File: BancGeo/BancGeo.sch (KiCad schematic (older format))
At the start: 114 parts, among them P1 Alim, P2 Batt, P3 CONN_01X05, P4 Capt1, P5 Capt2, P6 Capt3, P7 Capt4, P8 USB_D-, P9 USB_D+, Q1 2N7002E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

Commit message: Update Bancgeo
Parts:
- added R36: nc, Yame_library:SM0603-MR, symbol R
- D3, D4, D5, D7, D8, D9: footprint LEDs:LED-5MM -> Yame_library:LED-5MM_center
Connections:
- wire segments 374 -> 405
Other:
- moved on the sheet: R38, R39, R40, R41, R42, R43

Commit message: Update BancGeo
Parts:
- added C36: 100n, Yame_library:SM0603-MR, symbol C
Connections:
- net labels added: Self_Out_1, Self_Out_2, TR_High_Side, TR_Low_Side
- wire segments 405 -> 406
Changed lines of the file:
@@
 $EndComp
 Text Label 4150 4650 0    60   ~ 0
-+Vref1
++Vref2
 $Comp
 L R R11
@@
 	4050 1050 4300 1050
 Wire Wire Line
-	4700 900  4700 1050
+	4700 900  4700 1150
 Wire Wire Line
 	4700 1050 4600 1050
@@
 Wire Wire Line
 	13000 1700 12950 1700
+$Comp
+L C C36
+U 1 1 573E302E
+P 4700 1300
+F 0 "C36" H 4725 1400 50  0000 L CNN
+F 1 "100n" H 4725 1200 50  0000 L CNN
+F 2 "Yame_library:SM0603-MR" H 4738 1150 30  0001 C CNN
+F 3 "" H 4700 1300 60  0000 C CNN
+	1    4700 1300
+	1    0    0    -1
+$EndComp
+$Comp
+L GND #PWR070
+U 1 1 573E3034
+P 4700 1550
+F 0 "#PWR070" H 4700 1300 50  0001 C CNN
+F 1 "GND" H 4700 1400 50  0000 C CNN
+F 2 "" H 4700 1550 60  0000 C CNN
+F 3 "" H 4700 1550 60  0000 C CNN
+	1    4700 1550
+	1    0    0    -1
+$EndComp
+Wire Wire Line
+	4700 1450 4700 1550
+Connection ~ 4700 1050
+Text Label 5700 8000 0    60   ~ 0
+TR_Low_Side
+Text Label 5700 7300 0    60   ~ 0
+TR_High_Side
+Text Label 6350 7400 0    60   ~ 0
+Self_Out_2
+Text Label 6850 7900 0    60   ~ 0
+Self_Out_1
 $EndSCHEMATC

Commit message: Update BancGeo
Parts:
- added P10: GND, Yame_library:Test_Point_T_H, symbol CONN_01X01
- added Q6: 2N7002E, Yame_library:SOT23-MR, symbol N-MOS_SOT23
- added R37, R44: 100k, Yame_library:SM0603-MR, symbol R
- P1, P2: footprint Connect:PINHEAD1-2 -> Yame_library:PINHEAD1-2
- P4, P5, P6, P7: footprint Connect:PINHEAD1-3 -> Yame_library:PINHEAD1-3
- R1: value 10k -> 100k
- U3: value MCP6541 -> MCP6546
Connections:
- wire segments 406 -> 407
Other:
- moved on the sheet: Q1, R1

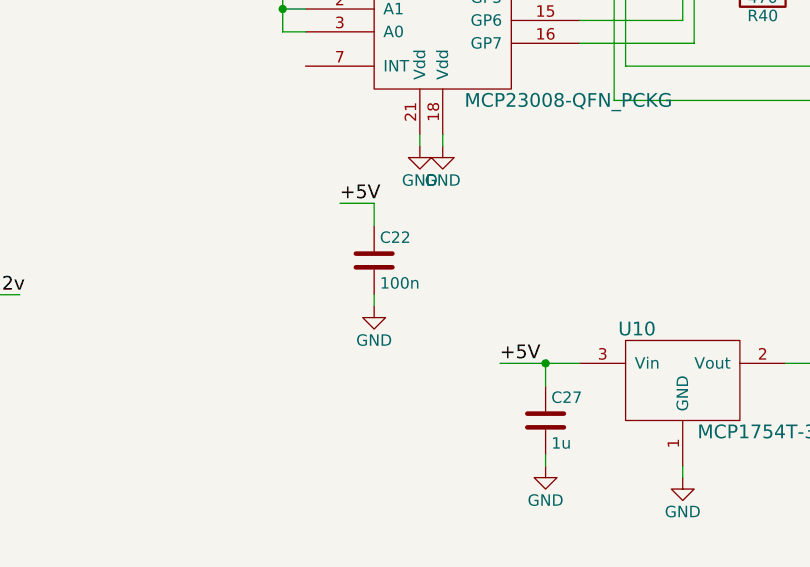
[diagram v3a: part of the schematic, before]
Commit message: Change C22 value
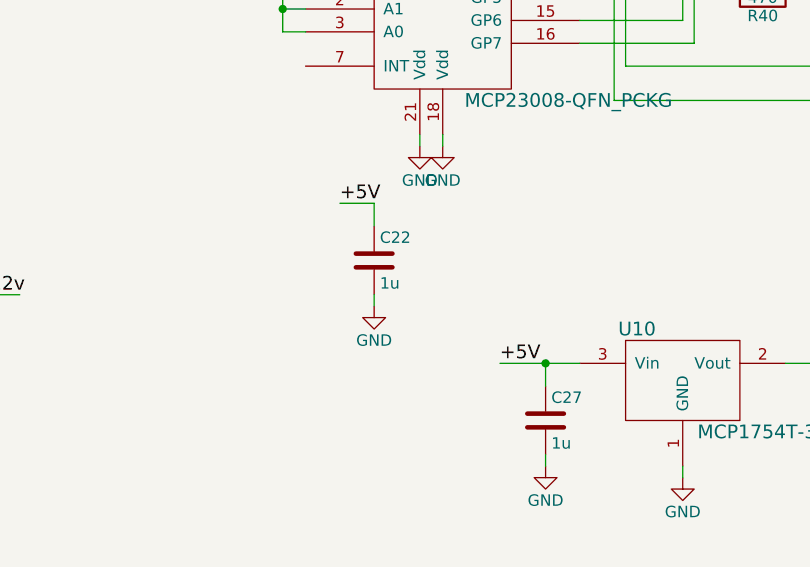
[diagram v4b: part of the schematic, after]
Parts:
- C22: value 100n -> 1u
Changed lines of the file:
@@
 P 12050 2950
 F 0 "C22" H 12075 3050 50  0000 L CNN
-F 1 "100n" H 12075 2850 50  0000 L CNN
+F 1 "1u" H 12075 2850 50  0000 L CNN
 F 2 "Yame_library:SM0805-MR" H 12088 2800 30  0001 C CNN
 F 3 "" H 12050 2950 60  0000 C CNN

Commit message: update Bancgeo.sch
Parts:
- U6: value MCP1631X-ML_QFN -> MCP1631V-ML_QFN
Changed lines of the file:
@@
 P 4950 9500
 F 0 "U6" H 2650 10850 60  0000 C CNN
-F 1 "MCP1631X-ML_QFN" H 3600 9050 60  0000 C CNN
+F 1 "MCP1631V-ML_QFN" H 3600 9050 60  0000 C CNN
 F 2 "Housings_DFN_QFN:QFN-20-1EP_4x4mm_Pitch0.5mm" H 4950 9500 60  0001 C CNN
 F 3 "" H 4950 9500 60  0000 C CNN

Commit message: Update BancGeo alim feed
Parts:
- added D? (x2): PDS760-13, symbol DIODE_SCHOTTKY_3PIN
- added Q?: P-MOS_SOIC, symbol P-MOS_SOIC
- added R?: 100k, symbol R
- D3, D4, D5, D6, D7, D8, D9: symbol LED -> LED-RESCUE-BancGeo
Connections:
- net labels added: +Vfeed
- wire segments 407 -> 426
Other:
- moved on the sheet: P2
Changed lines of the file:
@@
 EESchema Schematic File Version 2
+LIBS:BancGeo-rescue
 LIBS:power
 LIBS:device
@@
 Text Label 10300 3100 0    60   ~ 0
 +12v
-Text Label 7250 5400 0    60   ~ 0
+Text Label 2200 3300 0    60   ~ 0
 +Vbat
 $Comp
@@
 L CONN_01X02 P2
 U 1 1 56B94194
-P 1100 3850
-F 0 "P2" H 1100 4000 50  0000 C CNN
-F 1 "Batt" V 1200 3850 50  0000 C CNN
-F 2 "Yame_library:PINHEAD1-2" H 1100 3850 60  0001 C CNN
-F 3 "" H 1100 3850 60  0000 C CNN
-	1    1100 3850
+P 800 3850
+F 0 "P2" H 800 4000 50  0000 C CNN
+F 1 "Batt" V 900 3850 50  0000 C CNN
+F 2 "Yame_library:PINHEAD1-2" H 800 3850 60  0001 C CNN
+F 3 "" H 800 3850 60  0000 C CNN
+	1    800  3850
 	-1   0    0    -1
 $EndComp
@@
 $EndComp
 $Comp
-L LED D3
+L LED-RESCUE-BancGeo D3
 U 1 1 56BAE8CB
 P 14550 700
@@
 $EndComp
 $Comp
-L LED D4
+L LED-RESCUE-BancGeo D4
 U 1 1 56BAEA55
 P 14750 950
@@
 $EndComp
 $Comp
-L LED D5
+L LED-RESCUE-BancGeo D5
 U 1 1 56BAF1D5
 P 14950 1200
@@
 $EndComp
 $Comp
-L LED D7
+L LED-RESCUE-BancGeo D7
 U 1 1 56BAF1DB
 P 15100 1450
@@
 $EndComp
 $Comp
-L LED D8
+L LED-RESCUE-BancGeo D8
 U 1 1 56BAF1E1
 P 15300 1700
@@
 $EndComp
 $Comp
-L LED D9
+L LED-RESCUE-BancGeo D9
 U 1 1 56BAF1E7
 P 15500 1950
@@
 $EndComp
 $Comp
-L LED D6
+L LED-RESCUE-BancGeo D6
 U 1 1 56BD4C8C
 P 15000 6650
@@
 	9200 5400 8550 5400
 Wire Wire Line
-	1300 3900 1350 3900
+	1350 2900 1350 4000
 Wire Wire Line
-	1350 3900 1350 4000
-Wire Wire Line
-	1300 3800 2200 3800
+	1000 3800 2200 3800
 Wire Wire Line
 	1400 650  1900 650
@@
 Wire Wire Line
 	13100 1600 13100 2250
+$Comp
+L GND #PWR?
+U 1 1 58A8AD90
+P 1000 4000
+F 0 "#PWR?" H 1000 3750 50  0001 C CNN
+F 1 "GND" H 1000 3850 50  0000 C CNN
+F 2 "" H 1000 4000 60  0000 C CNN
+F 3 "" H 1000 4000 60  0000 C CNN
+	1    1000 4000
+	1    0    0    -1
+$EndComp
+Wire Wire Line
+	1000 3900 1000 4000
+$Comp
+L P-MOS_SOIC Q?
+U 1 1 58A8B1D3
+P 1700 2800
+F 0 "Q?" H 1500 2850 50  0000 L BNN
+F 1 "P-MOS_SOIC" H 1850 2750 50  0000 L BNN
+F 2 "" H 1700 2950 50  0001 C CNN
+F 3 "" H 1700 2800 60  0000 C CNN
+	1    1700 2800
+	1    0    0    -1
+$EndComp
+Wire Wire Line
+	1350 2900 1500 2900
+$Comp
+L R R?
+U 1 1 58A8C1CB
+P 1550 3300
+F 0 "R?" V 1630 3300 50  0000 C CNN
+F 1 "100k" V 1550 3300 50  0000 C CNN
+F 2 "" V 1480 3300 50  0000 C CNN
+F 3 "" H 1550 3300 50  0000 C CNN
+	1    1550 3300
+	0    1    1    0
+$EndComp
+Wire Wire Line
+	1700 3300 2450 3300
+Wire Wire Line
+	1800 3300 1800 3050
+Wire Wire Line
+	1950 3300 1950 3050
+Connection ~ 1800 3300
+Wire Wire Line
+	2100 3300 2100 3050
+Connection ~ 1950 3300
+Wire Wire Line
+	1400 3300 1350 3300
+Connection ~ 1350 3300
+Connection ~ 2100 3300
+Wire Wire Line
+	1800 2550 1800 2450
+Wire Wire Line
+	1800 2450 2450 2450
+Wire Wire Line
+	2250 2550 2250 2450
+Connection ~ 2250 2450
+Wire Wire Line
+	2100 2550 2100 2450
+Connection ~ 2100 2450
+Wire Wire Line
+	1950 2550 1950 2450
+Connection ~ 1950 2450
+Text Label 2300 2450 0    60   ~ 0
++Vfeed
+Text Label 6200 5150 0    60   ~ 0
++Vfeed
+$Comp
+L DIODE_SCHOTTKY_3PIN D?
+U 1 1 58A8F0BC
+P 6950 5600
+F 0 "D?" H 6950 5750 60  0000 C CNN
+F 1 "PDS760-13" H 7050 5450 60  0000 C CNN
+F 2 "" H 6950 5600 60  0000 C CNN
+F 3 "" H 6950 5600 60  0000 C CNN
+	1    6950 5600
+	1    0    0    -1
+$EndComp
+$Comp
+L DIODE_SCHOTTKY_3PIN D?
+U 1 1 58A8F35D
+P 6900 5150
+F 0 "D?" H 6900 5300 60  0000 C CNN
+F 1 "PDS760-13" H 7000 5000 60  0000 C CNN
+F 2 "" H 6900 5150 60  0000 C CNN
+F 3 "" H 6900 5150 60  0000 C CNN
+	1    6900 5150
+	1    0    0    -1
+$EndComp
+Text Label 6200 5600 0    60   ~ 0
++12v
+Wire Wire Line
+	7200 5150 7250 5150
+Wire Wire Line
+	7250 5150 7250 5600
+Connection ~ 7250 5400
+Wire Wire Line
+	6700 5500 6600 5500
+Wire Wire Line
+	6600 5500 6600 5600
+Wire Wire Line
+	6200 5600 6700 5600
+Wire Wire Line
+	6650 5050 6600 5050
+Wire Wire Line
+	6600 5050 6600 5150
+Wire Wire Line
+	6200 5150 6650 5150
+Connection ~ 6600 5600
+Connection ~ 6600 5150
 $EndSCHEMATC

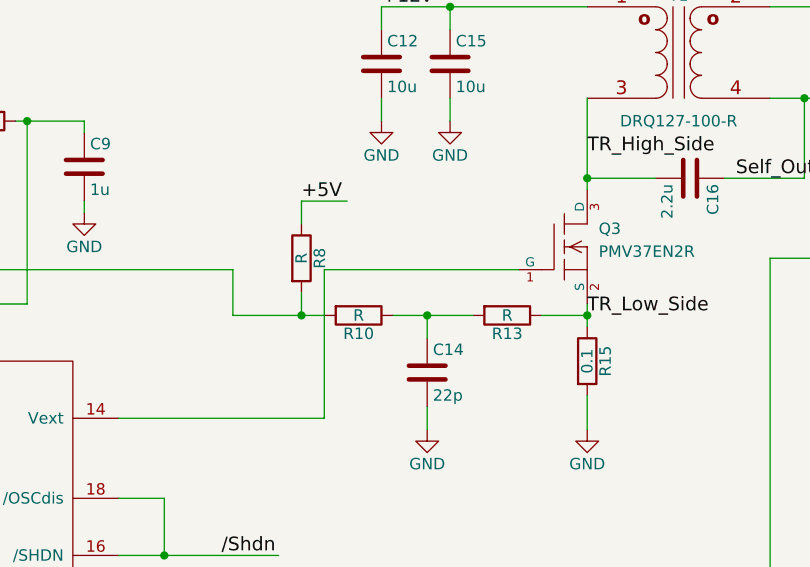
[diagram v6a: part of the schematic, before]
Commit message: Set L1 max current resistance values
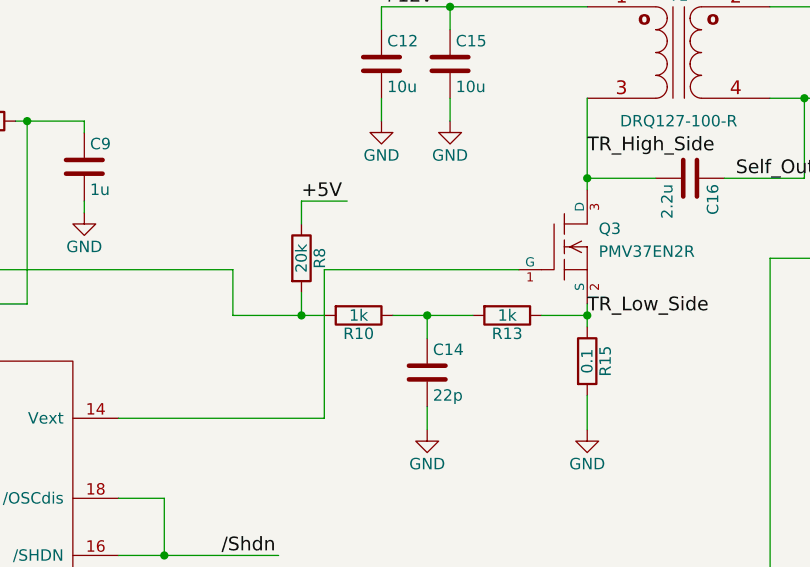
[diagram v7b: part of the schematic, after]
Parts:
- R10, R13: value R -> 1k
- R8: value R -> 20k
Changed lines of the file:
@@
 EESchema Schematic File Version 2
-LIBS:BancGeo-rescue
 LIBS:power
 LIBS:device
@@
 P 5350 8000
 F 0 "R13" V 5430 8000 50  0000 C CNN
-F 1 "R" V 5350 8000 50  0000 C CNN
+F 1 "1k" V 5350 8000 50  0000 C CNN
 F 2 "Yame_library:SM0603-MR" V 5280 8000 30  0001 C CNN
 F 3 "" H 5350 8000 30  0000 C CNN
@@
 P 4700 8000
 F 0 "R10" V 4780 8000 50  0000 C CNN
-F 1 "R" V 4700 8000 50  0000 C CNN
+F 1 "1k" V 4700 8000 50  0000 C CNN
 F 2 "Yame_library:SM0603-MR" V 4630 8000 30  0001 C CNN
 F 3 "" H 4700 8000 30  0000 C CNN
@@
 P 4450 7750
 F 0 "R8" V 4530 7750 50  0000 C CNN
-F 1 "R" V 4450 7750 50  0000 C CNN
+F 1 "20k" V 4450 7750 50  0000 C CNN
 F 2 "Yame_library:SM0603-MR" V 4380 7750 30  0001 C CNN
 F 3 "" H 4450 7750 30  0000 C CNN

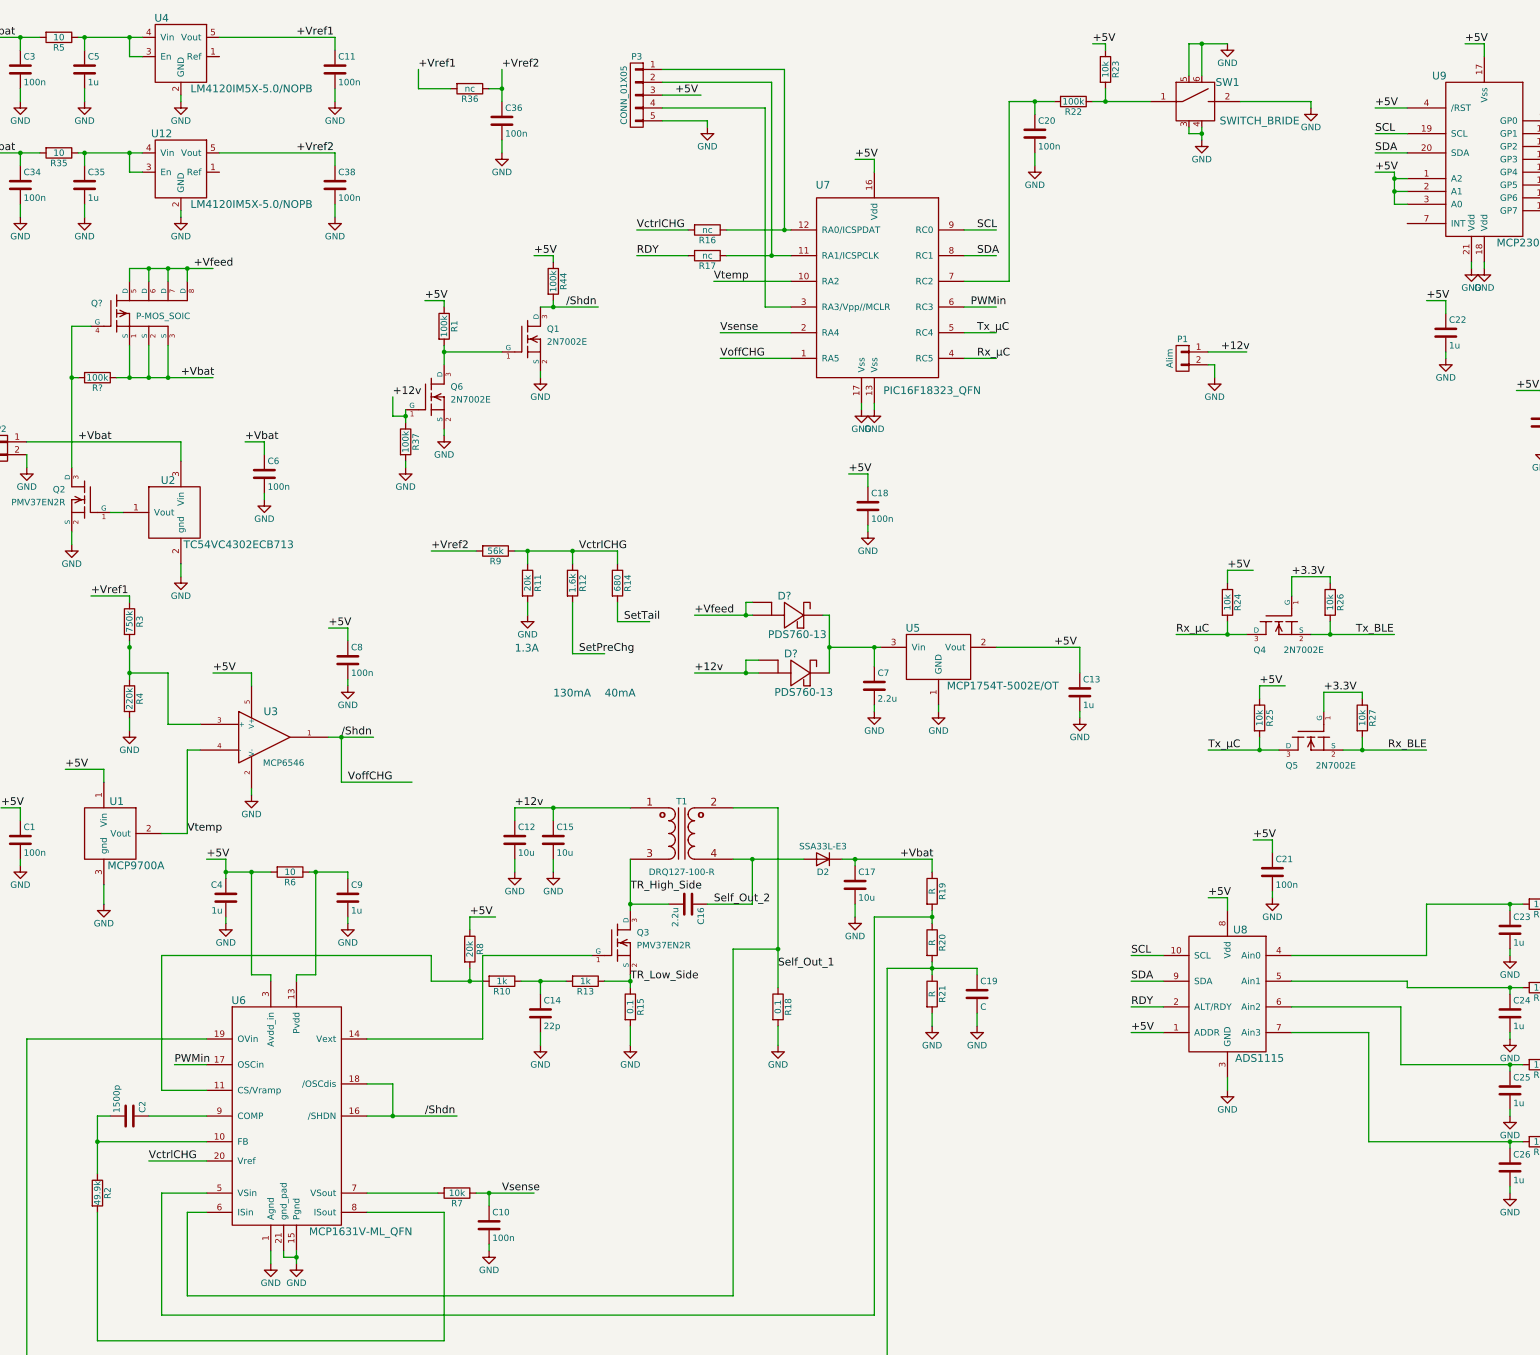
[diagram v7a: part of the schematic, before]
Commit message: Update bancgeo schematic : hotfix
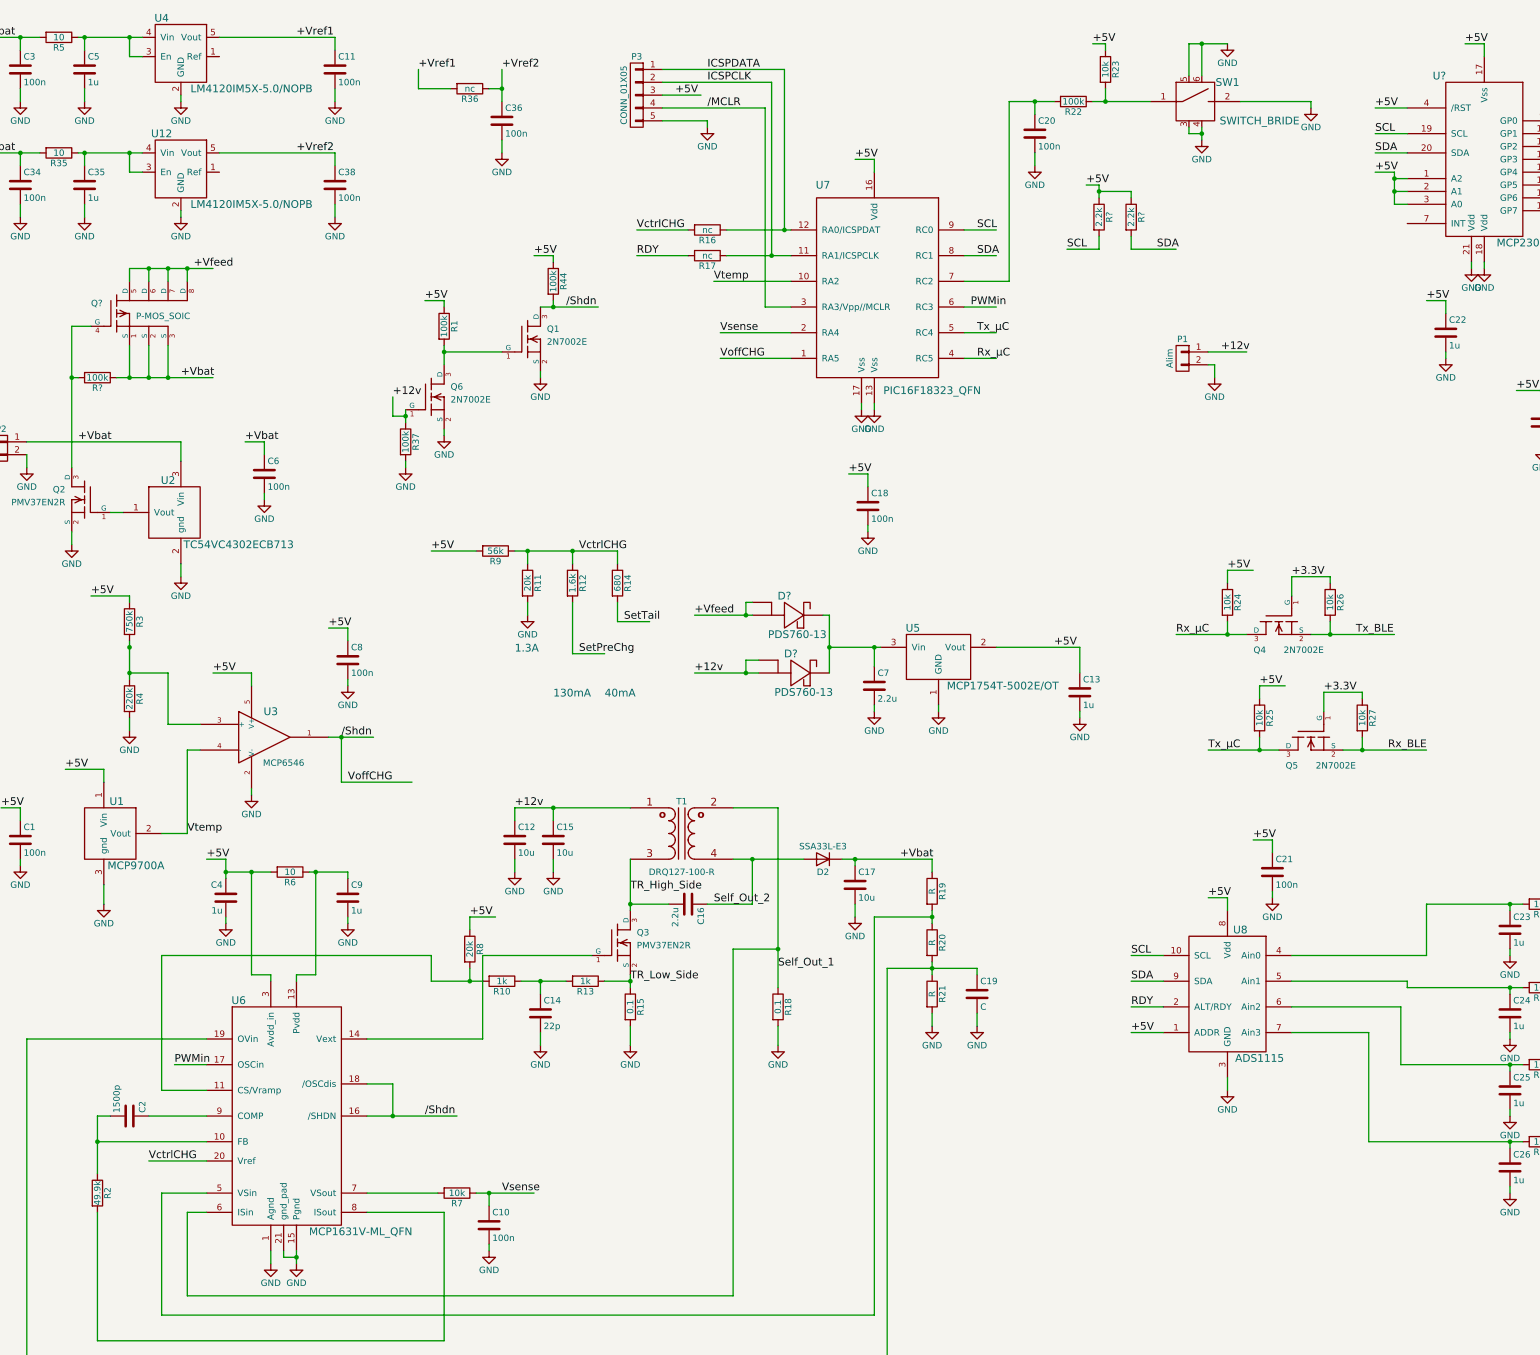
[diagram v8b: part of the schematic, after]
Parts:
- removed U9: MCP23008-QFN_PCKG, Housings_DFN_QFN:QFN-20-1EP_4x4mm_Pitch0.5mm, symbol MCP23008-QFN_PCKG
- added R? (x2): 2.2k, symbol R
- added U?: MCP23008-QFN_PCKG, symbol MCP23008-QFN_PCKG
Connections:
- net labels added: /MCLR, ICSPCLK, ICSPDATA
- wire segments 426 -> 434
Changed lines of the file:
@@
 $EndComp
 $Comp
-L MCP23008-QFN_PCKG U9
-U 1 1 56A54FC2
-P 12350 1650
-F 0 "U9" H 12000 2350 60  0000 C CNN
-F 1 "MCP23008-QFN_PCKG" H 12900 1050 60  0000 C CNN
-F 2 "Housings_DFN_QFN:QFN-20-1EP_4x4mm_Pitch0.5mm" H 12350 1650 60  0001 C CNN
-F 3 "" H 12350 1650 60  0000 C CNN
-	1    12350 1650
-	1    0    0    -1
-$EndComp
-$Comp
 L N-MOS_SOT23 Q3
 U 1 1 56B7BD68
@@
 Text Label 3100 650  0    60   ~ 0
 +Vref1
-Text Label 1500 5000 0    60   ~ 0
-+Vref1
 $Comp
 L GND #PWR022
@@
 	0    1    1    0
 $EndComp
-Text Label 4150 4650 0    60   ~ 0
-+Vref2
 $Comp
 L R R11
@@
 	1550 10800 1550 9800
 Wire Wire Line
-	3100 10200 3100 10100
+	3100 10100 3100 10200
 Wire Wire Line
 	2900 10100 2900 10200
@@
 Connection ~ 6600 5600
 Connection ~ 6600 5150
+Text Label 6300 1200 0    60   ~ 0
+/MCLR
+Text Label 6300 1000 0    60   ~ 0
+ICSPCLK
+Text Label 6300 900  0    60   ~ 0
+ICSPDATA
+$Comp
+L R R?
+U 1 1 58B982F4
+P 9350 2050
+F 0 "R?" V 9430 2050 50  0000 C CNN
+F 1 "2.2k" V 9350 2050 50  0000 C CNN
+F 2 "" V 9280 2050 50  0000 C CNN
+F 3 "" H 9350 2050 50  0000 C CNN
+	1    9350 2050
+	1    0    0    -1
+$EndComp
+Text Label 9250 1800 0    60   ~ 0
++5V
+Wire Wire Line
+	9250 1800 9350 1800
+Wire Wire Line
+	9350 1800 9350 1900
+$Comp
+L R R?
+U 1 1 58B98A00
+P 9600 2050
+F 0 "R?" V 9680 2050 50  0000 C CNN
+F 1 "2.2k" V 9600 2050 50  0000 C CNN
+F 2 "" V 9530 2050 50  0000 C CNN
+F 3 "" H 9600 2050 50  0000 C CNN
+	1    9600 2050
+	1    0    0    -1
+$EndComp
+Text Label 9100 2300 0    60   ~ 0
+SCL
+Text Label 9800 2300 0    60   ~ 0
+SDA
+Wire Wire Line
+	9100 2300 9350 2300
+Wire Wire Line
+	9600 2300 9950 2300
+Wire Wire Line
+	9350 2300 9350 2200
+Wire Wire Line
+	9600 2200 9600 2300
+Wire Wire Line
+	9350 1850 9600 1850
+Wire Wire Line
+	9600 1850 9600 1900
+Connection ~ 9350 1850
+Text Label 1500 5000 0    60   ~ 0
++5V
+Text Label 4150 4650 0    60   ~ 0
++5V
+$Comp
+L MCP23008-QFN_PCKG U?
+U 1 1 58B97AC8
+P 12350 1650
+F 0 "U?" H 12000 2350 60  0000 C CNN
+F 1 "MCP23008-QFN_PCKG" H 12900 1050 60  0000 C CNN
+F 2 "" H 12350 1650 60  0000 C CNN
+F 3 "" H 12350 1650 60  0000 C CNN
+	1    12350 1650
+	1    0    0    -1
+$EndComp
 $EndSCHEMATC
